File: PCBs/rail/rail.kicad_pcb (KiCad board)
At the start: 2 copper layers, 58.5 x 34 mm, 3 parts

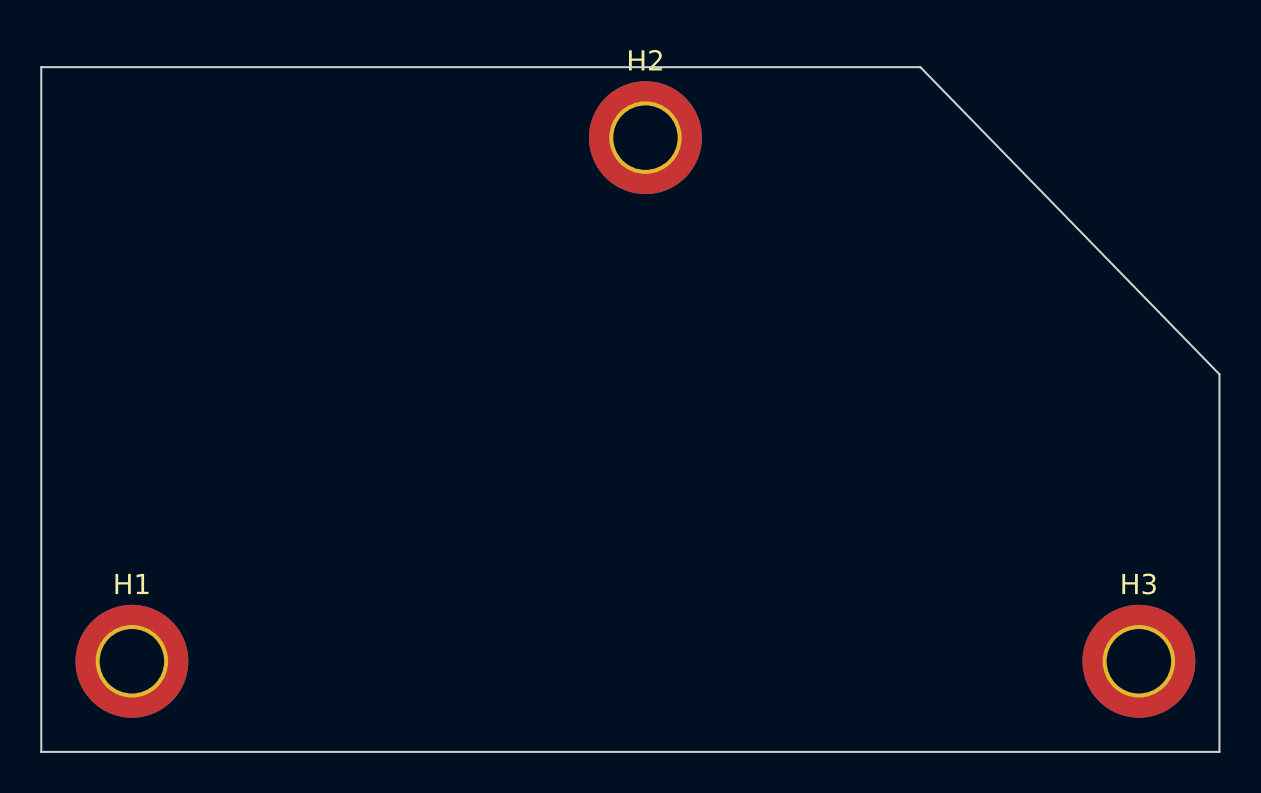
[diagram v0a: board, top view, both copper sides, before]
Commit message: Torso, bogie and rail complete. Next up: revise hand and IMU board in conjunction
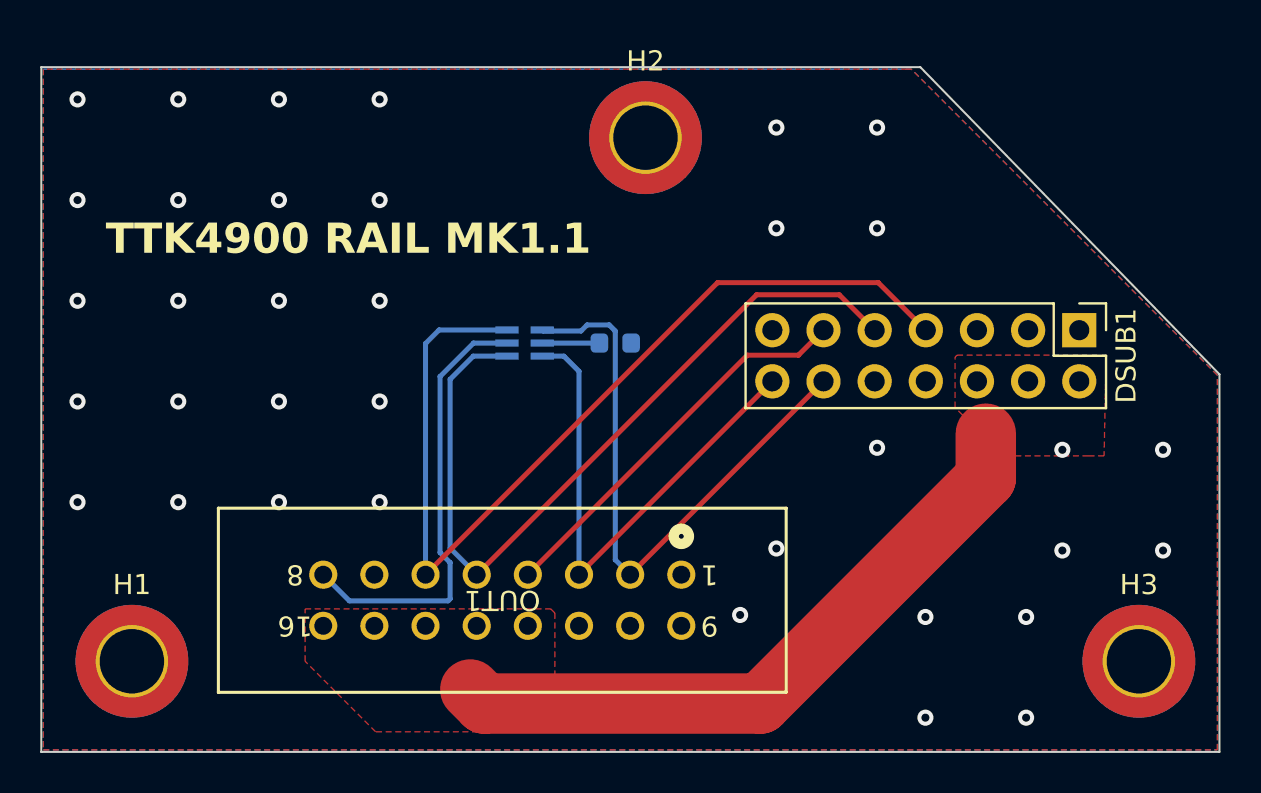
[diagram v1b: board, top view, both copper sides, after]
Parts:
- added CR1: CDSC706-0504C, CDSC706:CDSC706-0504C_BRN, B.Cu at (101.8, 60.9)
- added D1: LED, LED_SMD:LED_0603_1608Metric, B.Cu at (106.3, 60.9)
- added DSUB1: Conn_02x07_Odd_Even, Connector_PinHeader_2.54mm:PinHeader_2x07_P2.54mm_Vertical, F.Cu at (129.4, 60.3)
- added OUT1: Conn_02x08_Top_Bottom, 2-1761603-6:2-1761603-6_TYC, F.Cu at (109.6, 72.4)
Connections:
- H1 pad 1: unconnected-(H1-Pad1) -> GND
- H2 pad 1: unconnected-(H2-Pad1) -> GND
- H3 pad 1: unconnected-(H3-Pad1) -> GND
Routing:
- net /UART_TX: track 0.00 -> 47.6 mm
- net /UART_RX: track 0.00 -> 39.8 mm
- net +48V: track 0.00 -> 32.7 mm
- net /DP_OUT: track 0.00 -> 29.9 mm
- net /DM_OUT: track 0.00 -> 25.8 mm
- net +5V: track 0.00 -> 22.1 mm
- net /VB_OUT: track 0.00 -> 19.7 mm
- net Net-(D1-A): track 0.00 -> 2.84 mm
- net GND: vias 0 -> 35
- added copper zone on F.Cu, net +48V
- added copper zone on B.Cu, net GND
- added copper zone on F.Cu, net GND
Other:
- board text added: "G G G T R V G + + + G G P M"
- board text added: "G P M V R T G 5 G G G + + + + +"
- board text added: "KRISTIAN BLOM"
- board text added: "TTK4900 RAIL MK1.1"
